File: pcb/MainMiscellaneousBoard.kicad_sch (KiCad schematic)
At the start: 2 parts

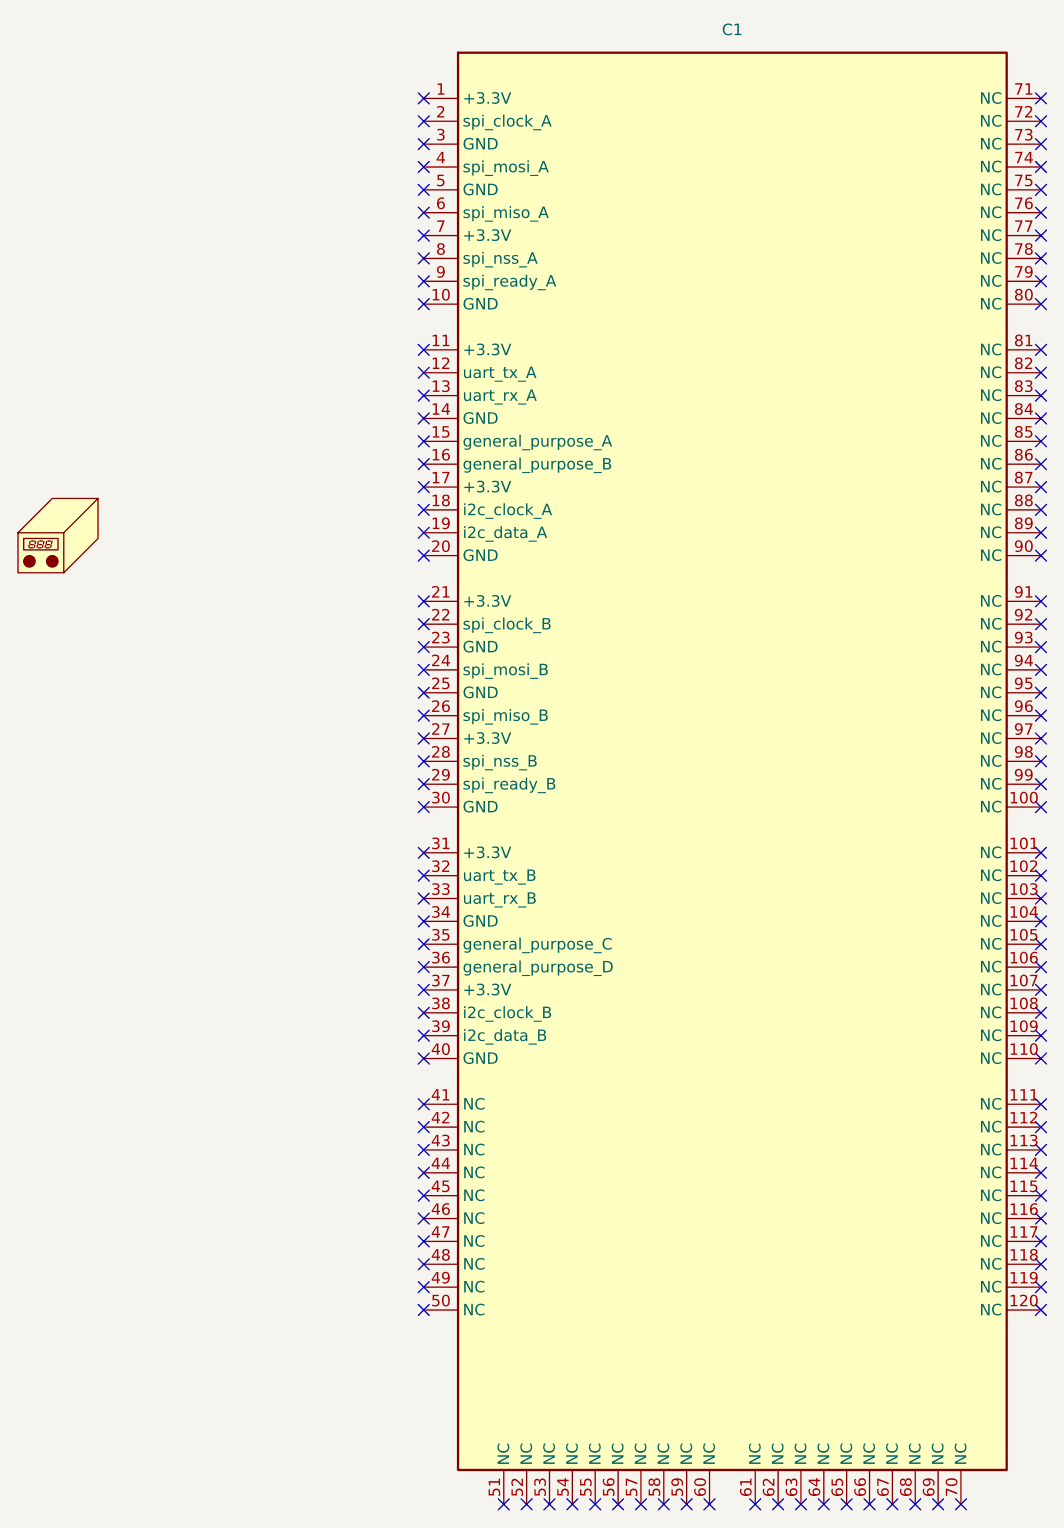
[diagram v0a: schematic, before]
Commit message: Updated main miscellaneous board with new stack-up layout.
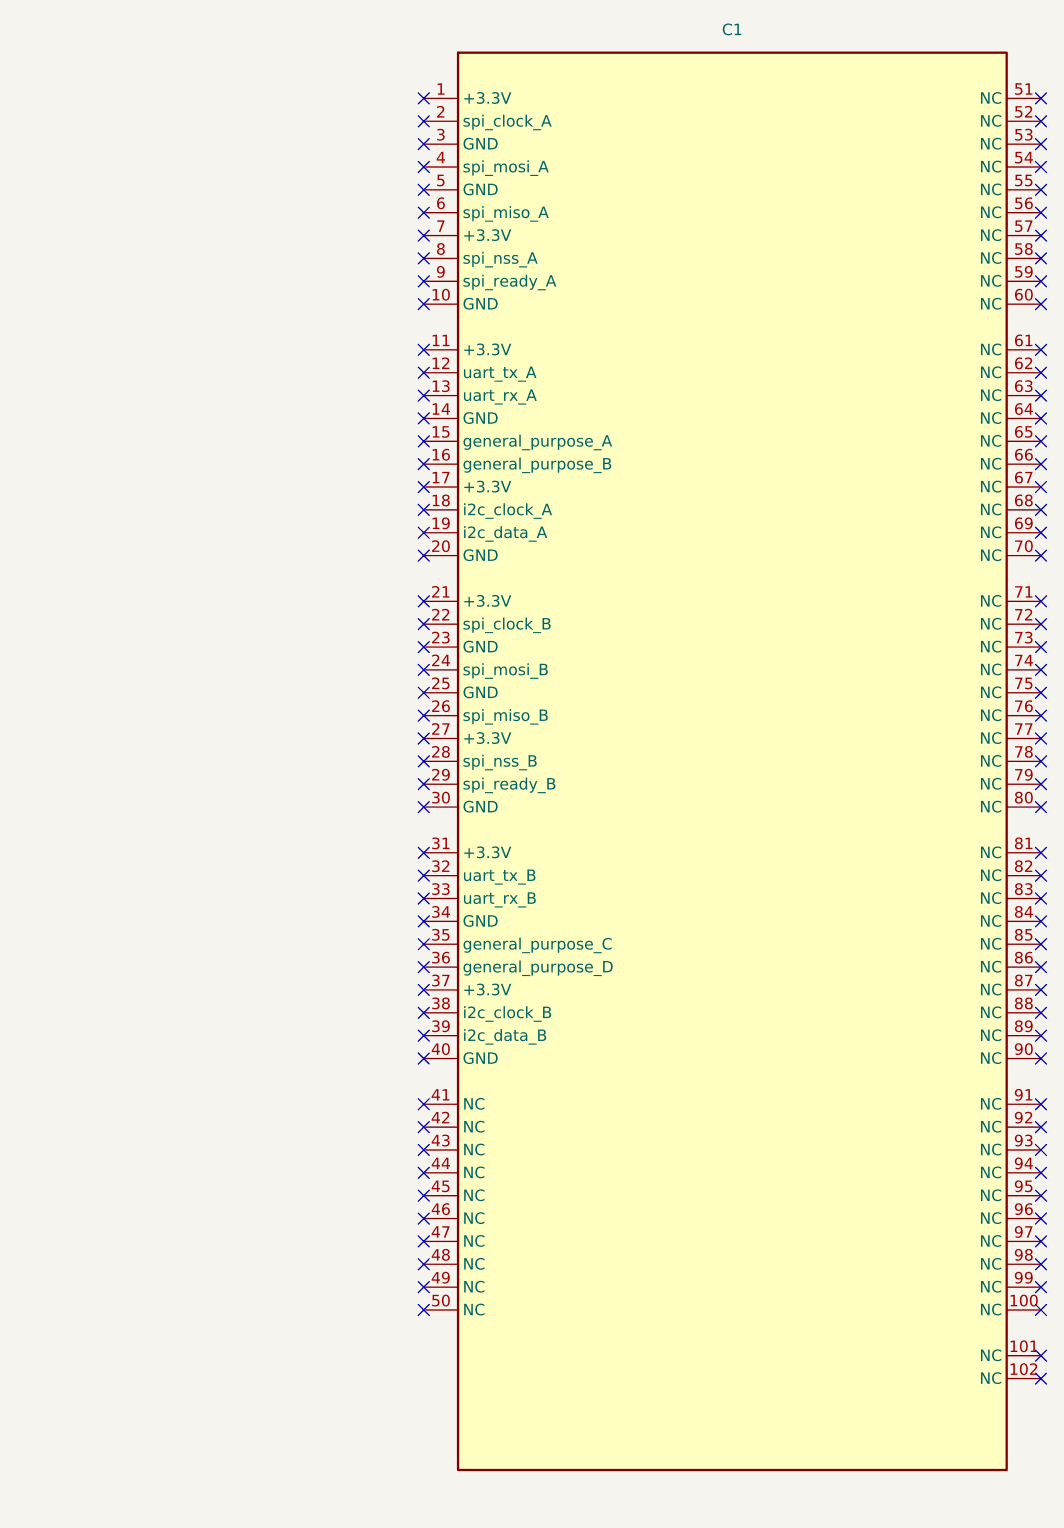
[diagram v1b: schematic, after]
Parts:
- removed N1: Housing, pcb:MainMiscellaneousBoardHousing, symbol Mechanical:Housing
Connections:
- no-connect marks 120 -> 102
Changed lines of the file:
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@@
 	(paper "A4")
 	(no_connect
-		(at 168.91 185.42)
-	)
-	(no_connect
 		(at 116.84 113.03)
 	)
@@
 	)
 	(no_connect
-		(at 156.21 185.42)
-	)
-	(no_connect
 		(at 185.42 128.27)
 	)
@@
 	)
 	(no_connect
-		(at 171.45 185.42)
-	)
-	(no_connect
 		(at 116.84 156.21)
 	)
@@
 	)
 	(no_connect
-		(at 173.99 185.42)
-	)
-	(no_connect
-		(at 130.81 185.42)
-	)
-	(no_connect
-		(at 153.67 185.42)
-	)
-	(no_connect
-		(at 143.51 185.42)
-	)
-	(no_connect
 		(at 116.84 153.67)
 	)
@@
 	)
 	(no_connect
-		(at 125.73 185.42)
-	)
-	(no_connect
 		(at 116.84 140.97)
 	)
@@
 	)
 	(no_connect
-		(at 161.29 185.42)
-	)
-	(no_connect
 		(at 185.42 31.75)
 	)
@@
 	)
 	(no_connect
-		(at 135.89 185.42)
+		(at 185.42 168.91)
 	)
 	(no_connect
@@
 	)
 	(no_connect
-		(at 148.59 185.42)
-	)
-	(no_connect
 		(at 116.84 97.79)
 	)
@@
 	)
 	(no_connect
-		(at 146.05 185.42)
-	)
-	(no_connect
 		(at 116.84 72.39)
 	)
@@
 	)
 	(no_connect
-		(at 133.35 185.42)
-	)
-	(no_connect
-		(at 158.75 185.42)
-	)
-	(no_connect
 		(at 185.42 105.41)
 	)
@@
 	)
 	(no_connect
-		(at 138.43 185.42)
-	)
-	(no_connect
 		(at 116.84 133.35)
 	)
@@
 	)
 	(no_connect
-		(at 166.37 185.42)
-	)
-	(no_connect
 		(at 116.84 120.65)
 	)
@@
 	)
 	(no_connect
-		(at 163.83 185.42)
-	)
-	(no_connect
 		(at 185.42 39.37)
 	)
@@
 	)
 	(no_connect
-		(at 128.27 185.42)
-	)
-	(no_connect
 		(at 185.42 146.05)
 	)
@@
 	)
 	(no_connect
-		(at 140.97 185.42)
-	)
-	(no_connect
 		(at 185.42 92.71)
 	)
@@
 	)
 	(no_connect
-		(at 176.53 185.42)
-	)
-	(no_connect
 		(at 185.42 77.47)
 	)
@@
 	(no_connect
 		(at 185.42 102.87)
+	)
+	(no_connect
+		(at 185.42 171.45)
 	)
 	(no_connect
@@
 			)
 		)
-		(pin "106"
-		)
 		(pin "10"
 		)
-		(pin "117"
-		)
 		(pin "3"
 		)
-		(pin "107"
-		)
 		(pin "36"
 		)
@@
 		(pin "41"
 		)
-		(pin "114"
-		)
 		(pin "33"
 		)
-		(pin "120"
-		)
 		(pin "11"
 		)
@@
 		(pin "68"
 		)
-		(pin "104"
-		)
-		(pin "115"
-		)
 		(pin "101"
 		)
@@
 		(pin "53"
 		)
-		(pin "113"
-		)
 		(pin "88"
 		)
-		(pin "111"
-		)
-		(pin "112"
-		)
 		(pin "9"
 		)
@@
 		(pin "91"
 		)
-		(pin "118"
-		)
 		(pin "48"
 		)
@@
 		(pin "13"
 		)
-		(pin "119"
-		)
 		(pin "57"
 		)
@@
 		(pin "40"
 		)
-		(pin "103"
-		)
 		(pin "16"
 		)
-		(pin "105"
-		)
 		(pin "99"
 		)
@@
 		(pin "80"
 		)
-		(pin "116"
-		)
-		(pin "110"
-		)
 		(pin "67"
 		)
@@
 		(pin "47"
 		)
-		(pin "108"
-		)
 		(pin "72"
 		)
@@
 		)
 		(pin "59"
-		)
-		(pin "109"
 		)
 		(pin "21"
@@
 					(unit 1)
 				)
-			)
-		)
-	)
-	(symbol
-		(lib_id "Mechanical:Housing")
-		(at 77.47 77.47 0)
-		(unit 1)
-		(exclude_from_sim no)
-		(in_bom yes)
-		(on_board yes)
-		(dnp no)
-		(fields_autoplaced yes)
-		(property "Reference" "N1"
-			(at 81.28 76.5174 0)
-			(effects
-				(font
-					(size 1.27 1.27)
-				)
-				(justify left)
-				(hide yes)
-			)
-		)
-		(property "Value" "Housing"
-			(at 81.28 79.0574 0)
-			(effects
-				(font
-					(size 1.27 1.27)
-				)
-				(justify left)
-				(hide yes)
-			)
-		)
-		(property "Footprint" "pcb:MainMiscellaneousBoardHousing"
-			(at 78.74 76.2 0)
-			(effects
-				(font
-					(size 1.27 1.27)
-				)
-				(hide yes)
-			)
-		)
-		(property "Datasheet" "~"
-			(at 78.74 76.2 0)
-			(effects
-				(font
-					(size 1.27 1.27)
-				)
-				(hide yes)
-			)
-		)
-		(property "Description" "Housing"
-			(at 77.47 77.47 0)
-			(effects
-				(font
-					(size 1.27 1.27)
-				)
-				(hide yes)
-			)
-		)
-		(instances
-			(project ""
-				(path "/98fc9565-7d66-4cd3-b0d6-fc60566bea9b"
-					(reference "N1")
-					(unit 1)
-				)

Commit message: uSD Connector (V6 : Hierarchical labels).
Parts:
- added C2: 1u, Capacitor_SMD:C_1206_3216Metric_Pad1.33x1.80mm_HandSolder, symbol Device:C_Small
- added C3: 100n, Capacitor_SMD:C_1206_3216Metric_Pad1.33x1.80mm_HandSolder, symbol Device:C_Small
- added C4: 10n, Capacitor_SMD:C_1206_3216Metric_Pad1.33x1.80mm_HandSolder, symbol Device:C_Small
- added J1: 0472192001, pcb:microSD_HC_Molex_47219-2001, symbol Connector:Micro_SD_Card
- added R1, R2, R3, R4, R5, R6: R_Small, Resistor_SMD:R_1206_3216Metric_Pad1.30x1.75mm_HandSolder, symbol Device:R_Small
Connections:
- new net: J1.1 (DAT2), R1.2
- new net: J1.5 (CLK), R2.2
- new net: J1.2 (DAT3/CD), R4.2
- new net: J1.7 (DAT0), R3.2
- new net: J1.3 (CMD), R6.2
- new net: J1.8 (DAT1), R5.2
- new net +3.3V: C2.1, C3.1, C4.1, J1.4 (VDD)
- new net GND: C2.2, C3.2, C4.2, J1.6 (VSS), J1.9 (SHIELD)
- new net clock: R2.1
- new net cmd: R6.1
- new net data_0: R3.1
- new net data_1: R5.1
- new net data_2: R1.1
- new net data_3: R4.1
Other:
- note added: "uSD Connector (V6 : Hierarchical labels)."
- moved on the sheet: C1

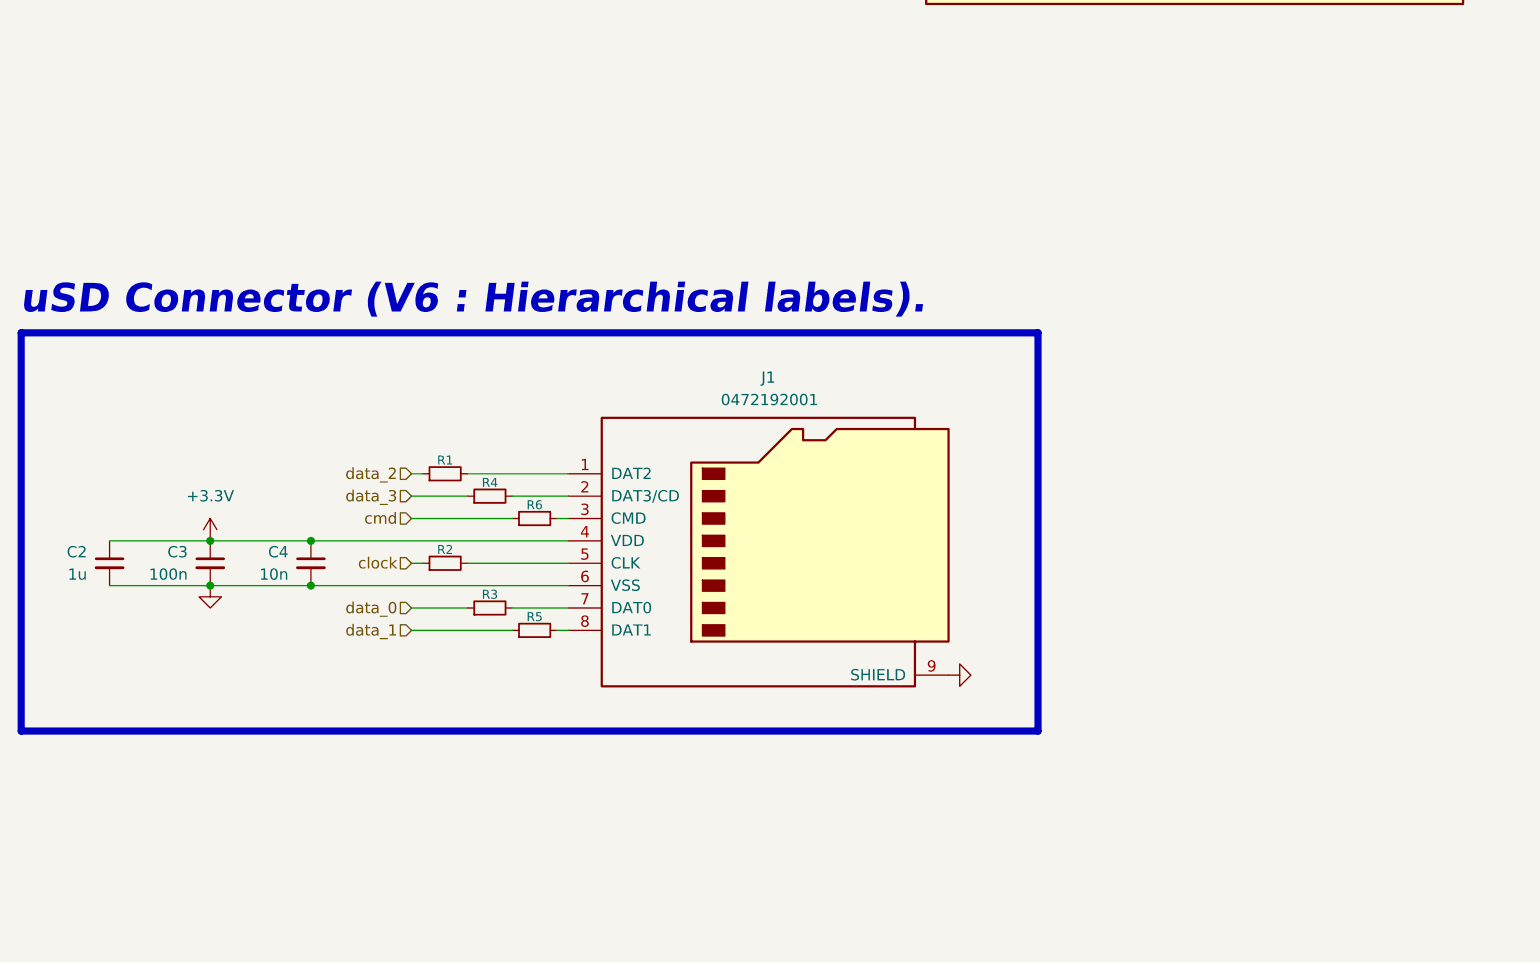
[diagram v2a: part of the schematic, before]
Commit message: Added uSD card connectors for camera subsystem A and B.
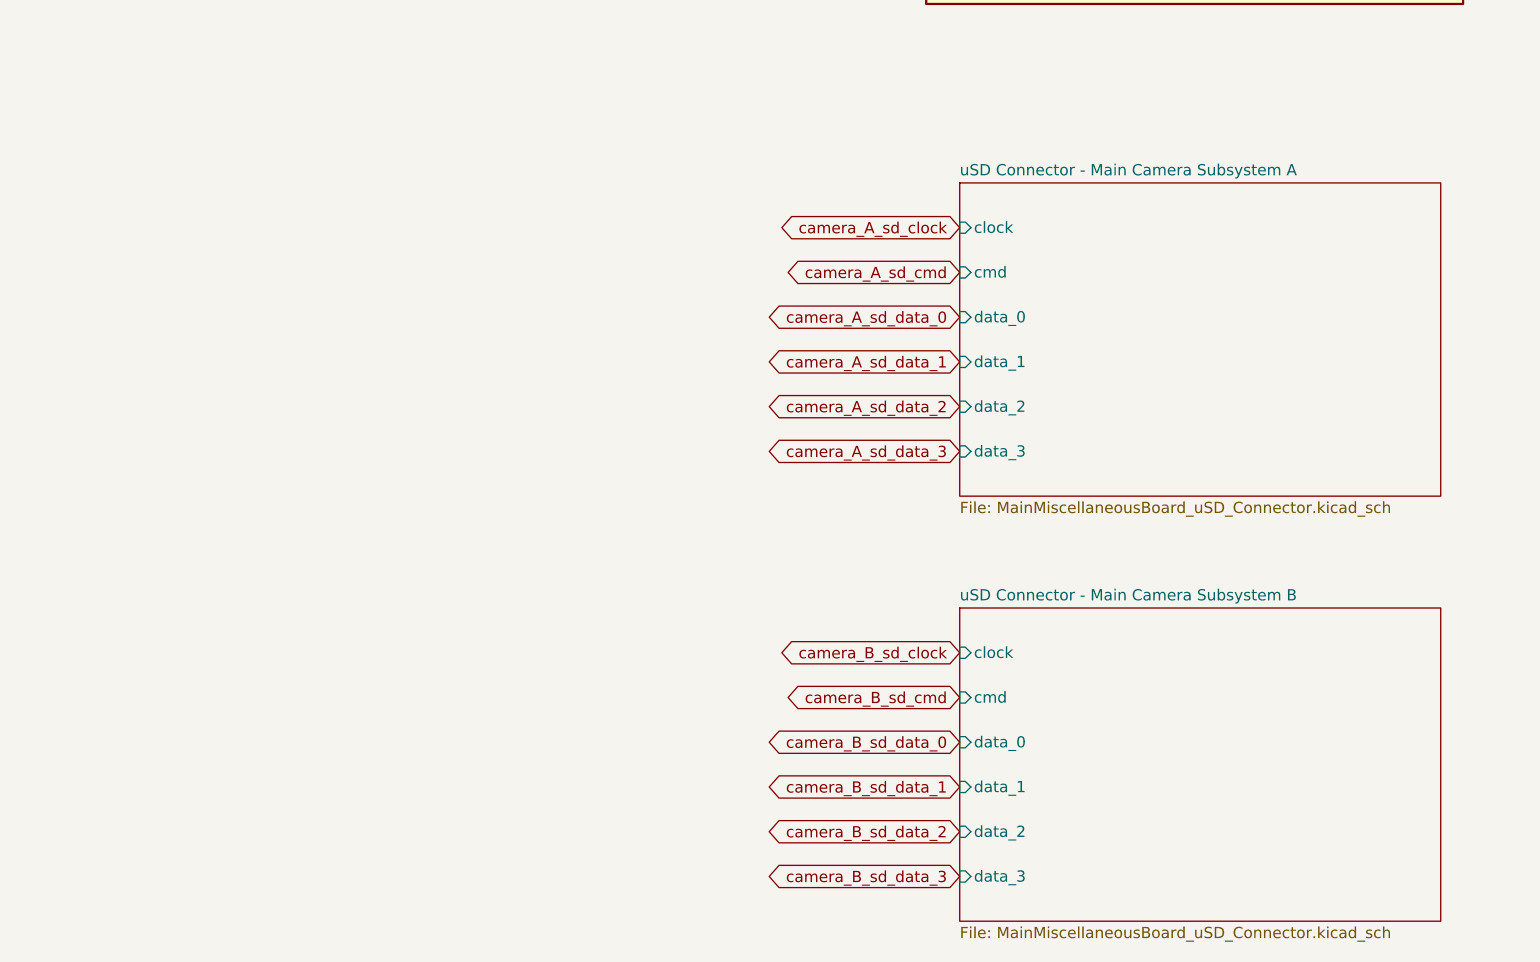
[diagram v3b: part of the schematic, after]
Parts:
- removed C2: 1u, Capacitor_SMD:C_1206_3216Metric_Pad1.33x1.80mm_HandSolder, symbol Device:C_Small
- removed C3: 100n, Capacitor_SMD:C_1206_3216Metric_Pad1.33x1.80mm_HandSolder, symbol Device:C_Small
- removed C4: 10n, Capacitor_SMD:C_1206_3216Metric_Pad1.33x1.80mm_HandSolder, symbol Device:C_Small
- removed J1: 0472192001, pcb:microSD_HC_Molex_47219-2001, symbol Connector:Micro_SD_Card
- removed R1, R2, R3, R4, R5, R6: R_Small, Resistor_SMD:R_1206_3216Metric_Pad1.30x1.75mm_HandSolder, symbol Device:R_Small
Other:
- added sheet uSD Connector - Main Camera Subsystem A (MainMiscellaneousBoard_uSD_Connector.kicad_sch)
- added sheet uSD Connector - Main Camera Subsystem B (MainMiscellaneousBoard_uSD_Connector.kicad_sch)
- note removed: "uSD Connector (V6 : Hierarchical labels)."

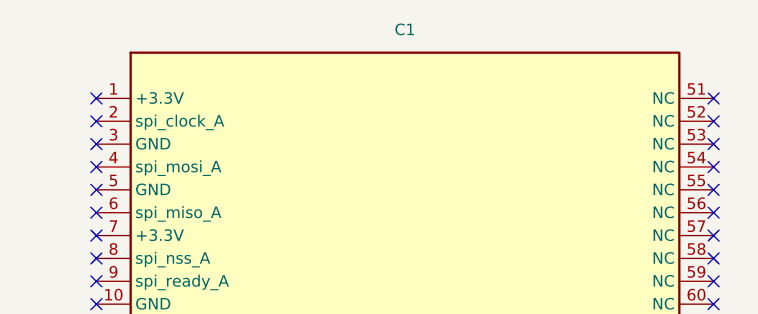
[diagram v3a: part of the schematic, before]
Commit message: Updated `StackConnector` to use reference prefix of "J".
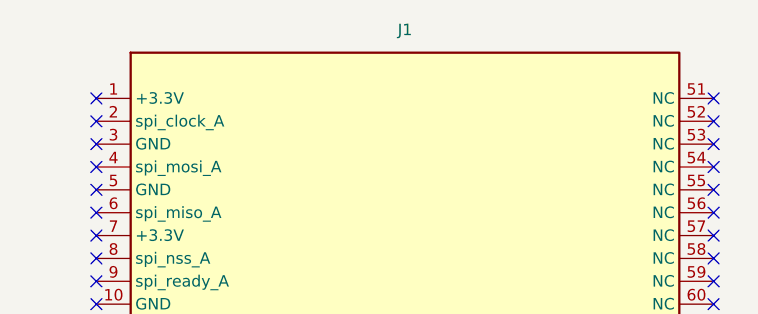
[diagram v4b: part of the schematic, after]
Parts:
- renumbered C1 to J1
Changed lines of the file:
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@@
 		(dnp no)
 		(fields_autoplaced yes)
-		(property "Reference" "C1"
+		(property "Reference" "J1"
 			(at 502.92 41.91 0)
 			(effects
@@
 			(project ""
 				(path "/98fc9565-7d66-4cd3-b0d6-fc60566bea9b"
-					(reference "C1")
+					(reference "J1")
 					(unit 1)
 				)
